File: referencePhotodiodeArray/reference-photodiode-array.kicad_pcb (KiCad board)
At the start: 2 copper layers, 28 x 28 mm, 19 parts

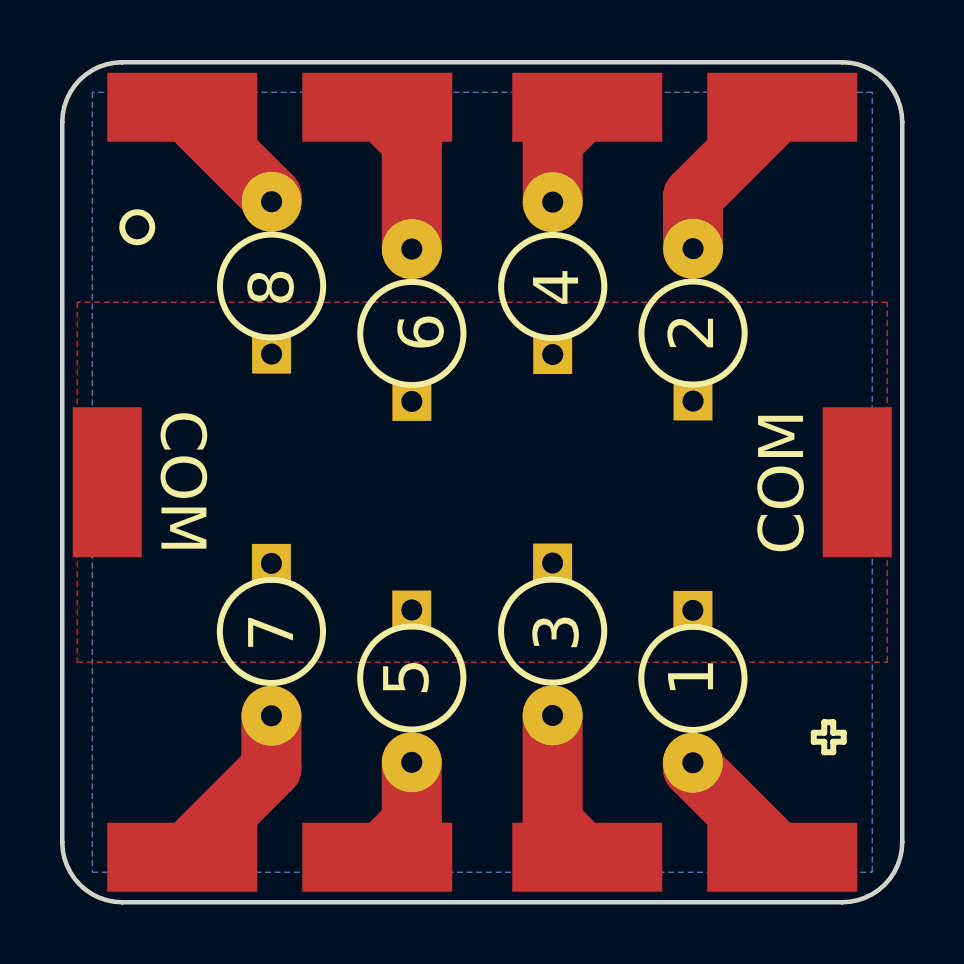
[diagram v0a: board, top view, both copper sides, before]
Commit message: put pads on both sides
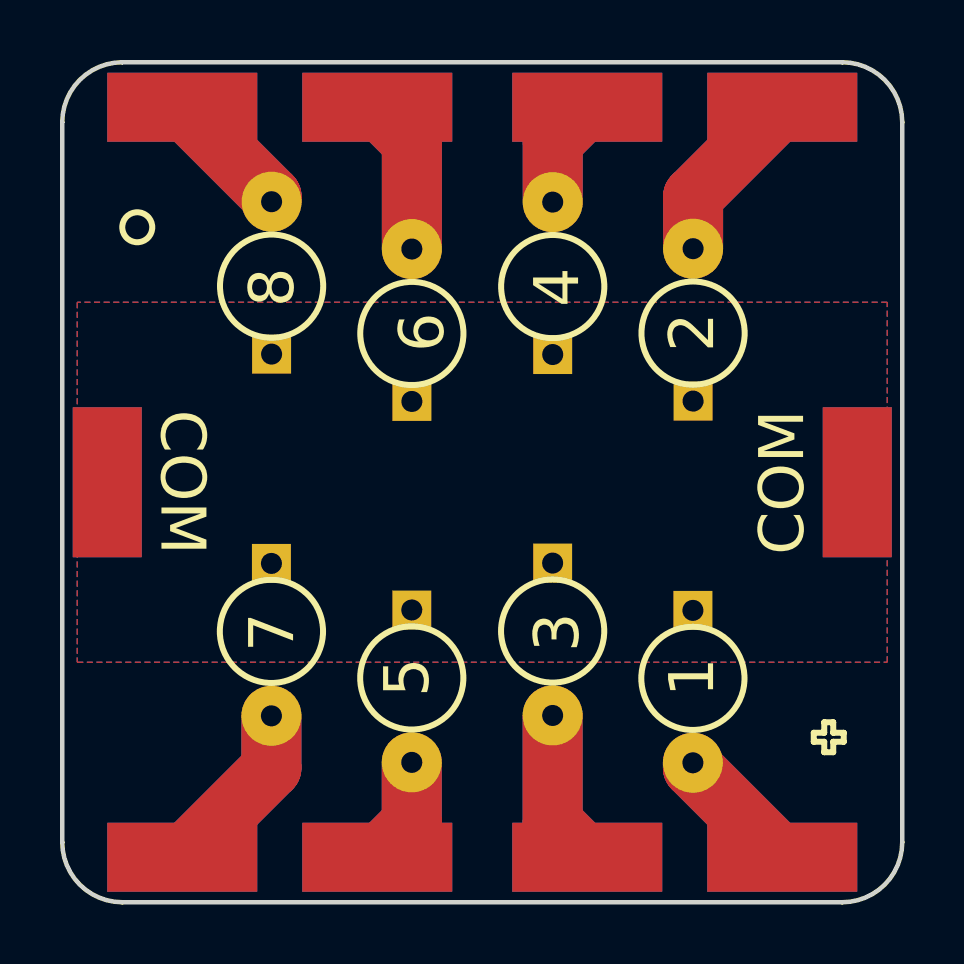
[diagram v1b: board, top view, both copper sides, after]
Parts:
- added W11: TEST_1P, testPad:SolderWirePad_single_SMD_5x2.3mm, B.Cu at (1.50, -14.0)
- added W12: TEST_1P, testPad:SolderWirePad_single_SMD_5x2.3mm, B.Cu at (4.00, -26.5)
- added W13: TEST_1P, testPad:SolderWirePad_single_SMD_5x2.3mm, B.Cu at (4.00, -1.50)
- added W14: TEST_1P, testPad:SolderWirePad_single_SMD_5x2.3mm, B.Cu at (10.5, -26.5)
- added W15: TEST_1P, testPad:SolderWirePad_single_SMD_5x2.3mm, B.Cu at (10.5, -1.50)
- added W16: TEST_1P, testPad:SolderWirePad_single_SMD_5x2.3mm, B.Cu at (17.5, -26.5)
- added W17: TEST_1P, testPad:SolderWirePad_single_SMD_5x2.3mm, B.Cu at (17.5, -1.50)
- added W18: TEST_1P, testPad:SolderWirePad_single_SMD_5x2.3mm, B.Cu at (24.0, -26.5)
- added W19: TEST_1P, testPad:SolderWirePad_single_SMD_5x2.3mm, B.Cu at (24.0, -1.50)
- added W20: TEST_1P, testPad:SolderWirePad_single_SMD_5x2.3mm, B.Cu at (26.5, -14.0)
- moved G*** 13.0 mm to (14.0, -14.0)
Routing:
- net Net-(D2-Pad2): track 5.95 -> 11.9 mm
- net Net-(D7-Pad2): track 5.95 -> 11.9 mm
- net Net-(D6-Pad2): track 5.20 -> 10.4 mm
- net Net-(D3-Pad2): track 5.20 -> 10.4 mm
- net Net-(D1-Pad2): track 4.38 -> 8.76 mm
- net Net-(D8-Pad2): track 4.38 -> 8.76 mm
- net Net-(D5-Pad2): track 3.64 -> 7.28 mm
- net Net-(D4-Pad2): track 3.64 -> 7.28 mm
